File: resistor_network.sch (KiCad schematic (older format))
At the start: 0 parts

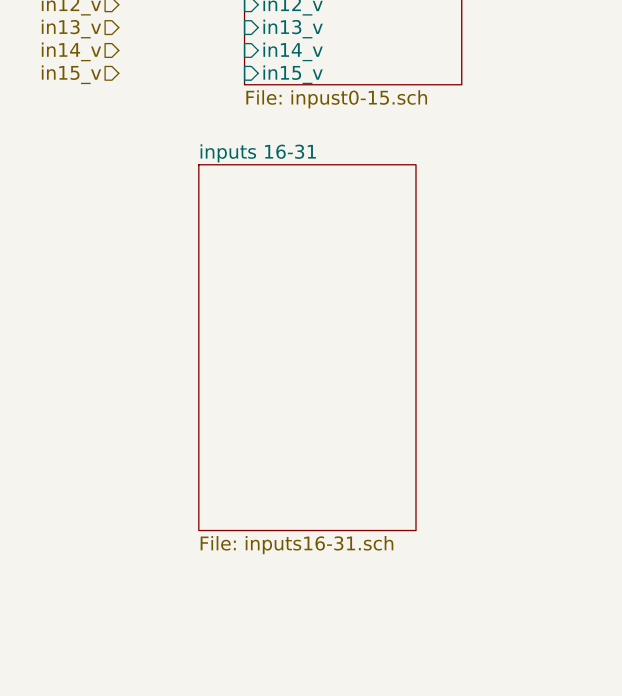
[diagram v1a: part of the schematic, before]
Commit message: added input/output for 16-31
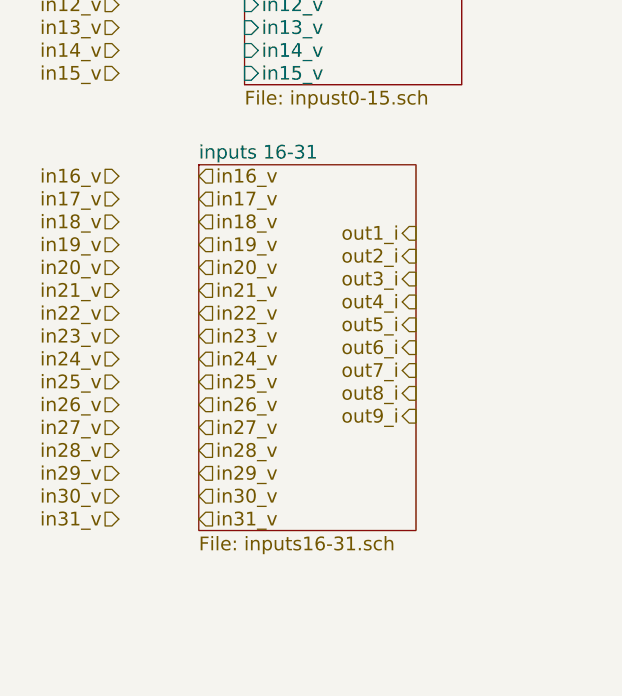
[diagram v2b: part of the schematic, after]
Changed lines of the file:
@@
 Text HLabel 1650 2600 0    60   Input ~ 0
 in15_v
+Text HLabel 1650 3050 0    60   Input ~ 0
+in16_v
+Text HLabel 1650 3150 0    60   Input ~ 0
+in17_v
+Text HLabel 1650 3250 0    60   Input ~ 0
+in18_v
+Text HLabel 1650 3350 0    60   Input ~ 0
+in19_v
+Text HLabel 1650 3450 0    60   Input ~ 0
+in20_v
+Text HLabel 1650 3550 0    60   Input ~ 0
+in21_v
+Text HLabel 1650 3650 0    60   Input ~ 0
+in22_v
+Text HLabel 1650 3750 0    60   Input ~ 0
+in23_v
+Text HLabel 1650 3850 0    60   Input ~ 0
+in24_v
+Text HLabel 1650 3950 0    60   Input ~ 0
+in25_v
+Text HLabel 1650 4050 0    60   Input ~ 0
+in26_v
+Text HLabel 1650 4150 0    60   Input ~ 0
+in27_v
+Text HLabel 1650 4250 0    60   Input ~ 0
+in28_v
+Text HLabel 1650 4350 0    60   Input ~ 0
+in29_v
+Text HLabel 1650 4450 0    60   Input ~ 0
+in30_v
+Text HLabel 1650 4550 0    60   Input ~ 0
+in31_v
+Text HLabel 2000 3050 2    60   Input ~ 0
+in16_v
+Text HLabel 2000 3150 2    60   Input ~ 0
+in17_v
+Text HLabel 2000 3250 2    60   Input ~ 0
+in18_v
+Text HLabel 2000 3350 2    60   Input ~ 0
+in19_v
+Text HLabel 2000 3450 2    60   Input ~ 0
+in20_v
+Text HLabel 2000 3550 2    60   Input ~ 0
+in21_v
+Text HLabel 2000 3650 2    60   Input ~ 0
+in22_v
+Text HLabel 2000 3750 2    60   Input ~ 0
+in23_v
+Text HLabel 2000 3850 2    60   Input ~ 0
+in24_v
+Text HLabel 2000 3950 2    60   Input ~ 0
+in25_v
+Text HLabel 2000 4050 2    60   Input ~ 0
+in26_v
+Text HLabel 2000 4150 2    60   Input ~ 0
+in27_v
+Text HLabel 2000 4250 2    60   Input ~ 0
+in28_v
+Text HLabel 2000 4350 2    60   Input ~ 0
+in29_v
+Text HLabel 2000 4450 2    60   Input ~ 0
+in30_v
+Text HLabel 2000 4550 2    60   Input ~ 0
+in31_v
+Text HLabel 2950 3300 0    60   Output ~ 0
+out1_i
+Text HLabel 2950 3400 0    60   Output ~ 0
+out2_i
+Text HLabel 2950 3500 0    60   Output ~ 0
+out3_i
+Text HLabel 2950 3600 0    60   Output ~ 0
+out4_i
+Text HLabel 2950 3700 0    60   Output ~ 0
+out5_i
+Text HLabel 2950 3800 0    60   Output ~ 0
+out6_i
+Text HLabel 2950 3900 0    60   Output ~ 0
+out7_i
+Text HLabel 2950 4000 0    60   Output ~ 0
+out8_i
+Text HLabel 2950 4100 0    60   Output ~ 0
+out9_i
 $EndSCHEMATC

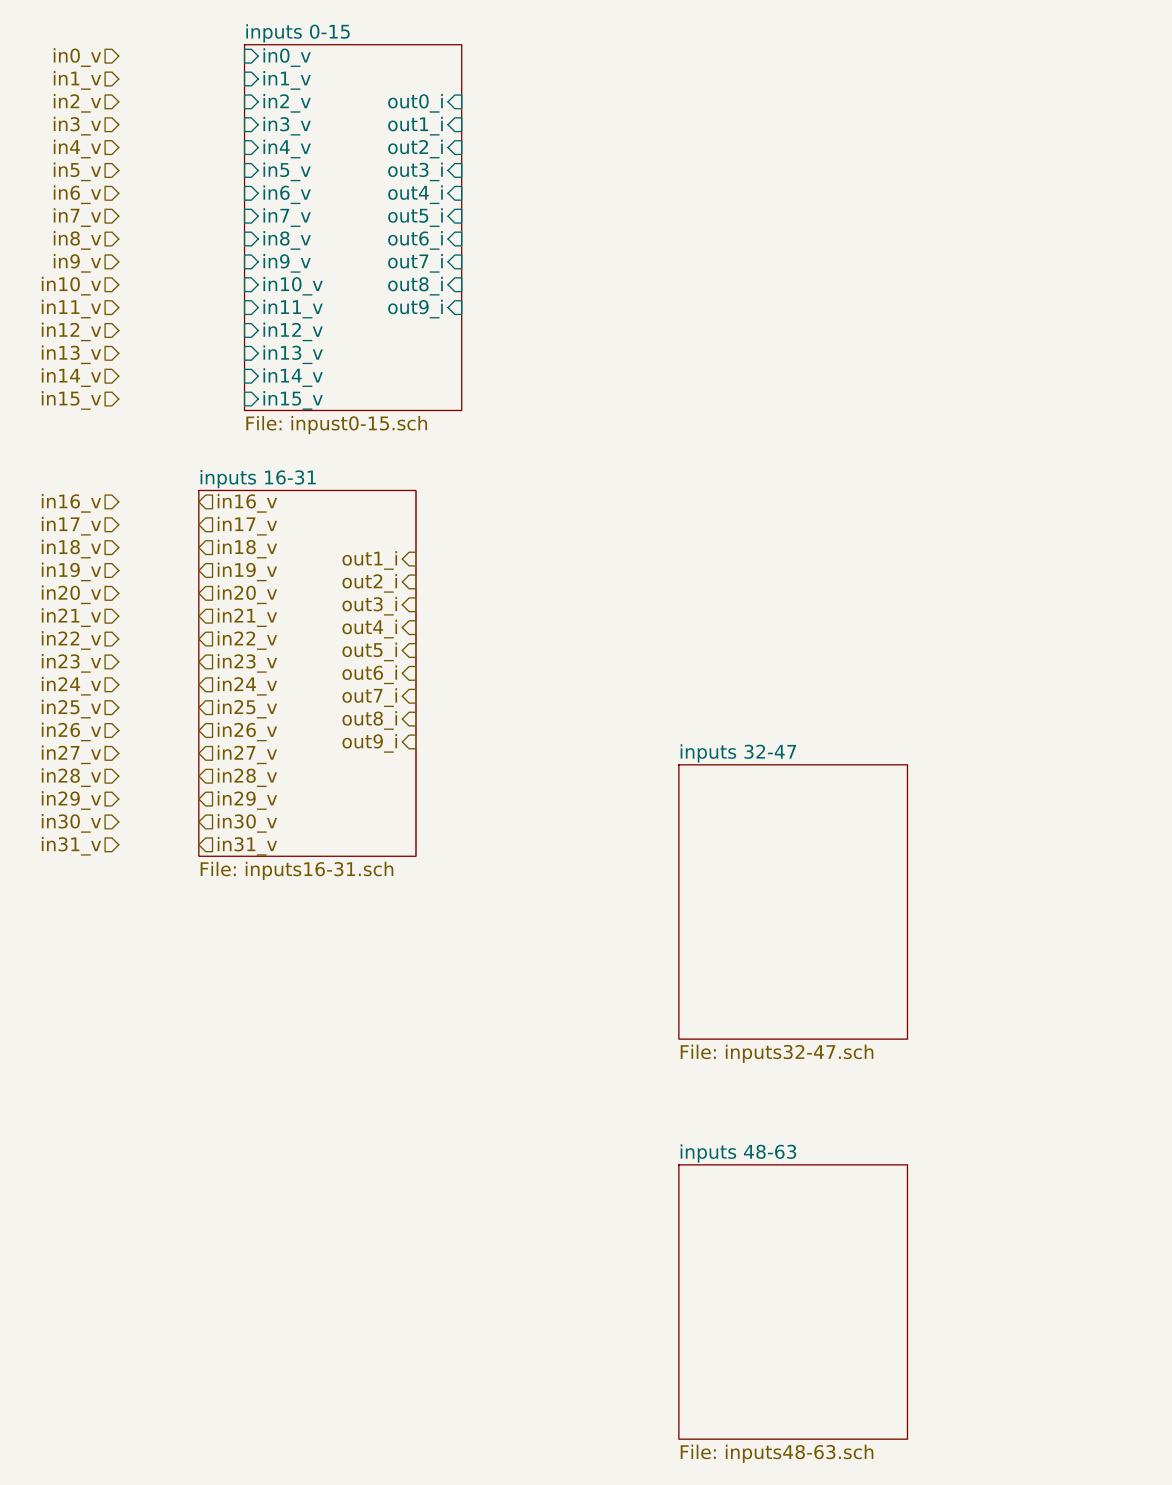
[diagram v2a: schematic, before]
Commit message: added labels
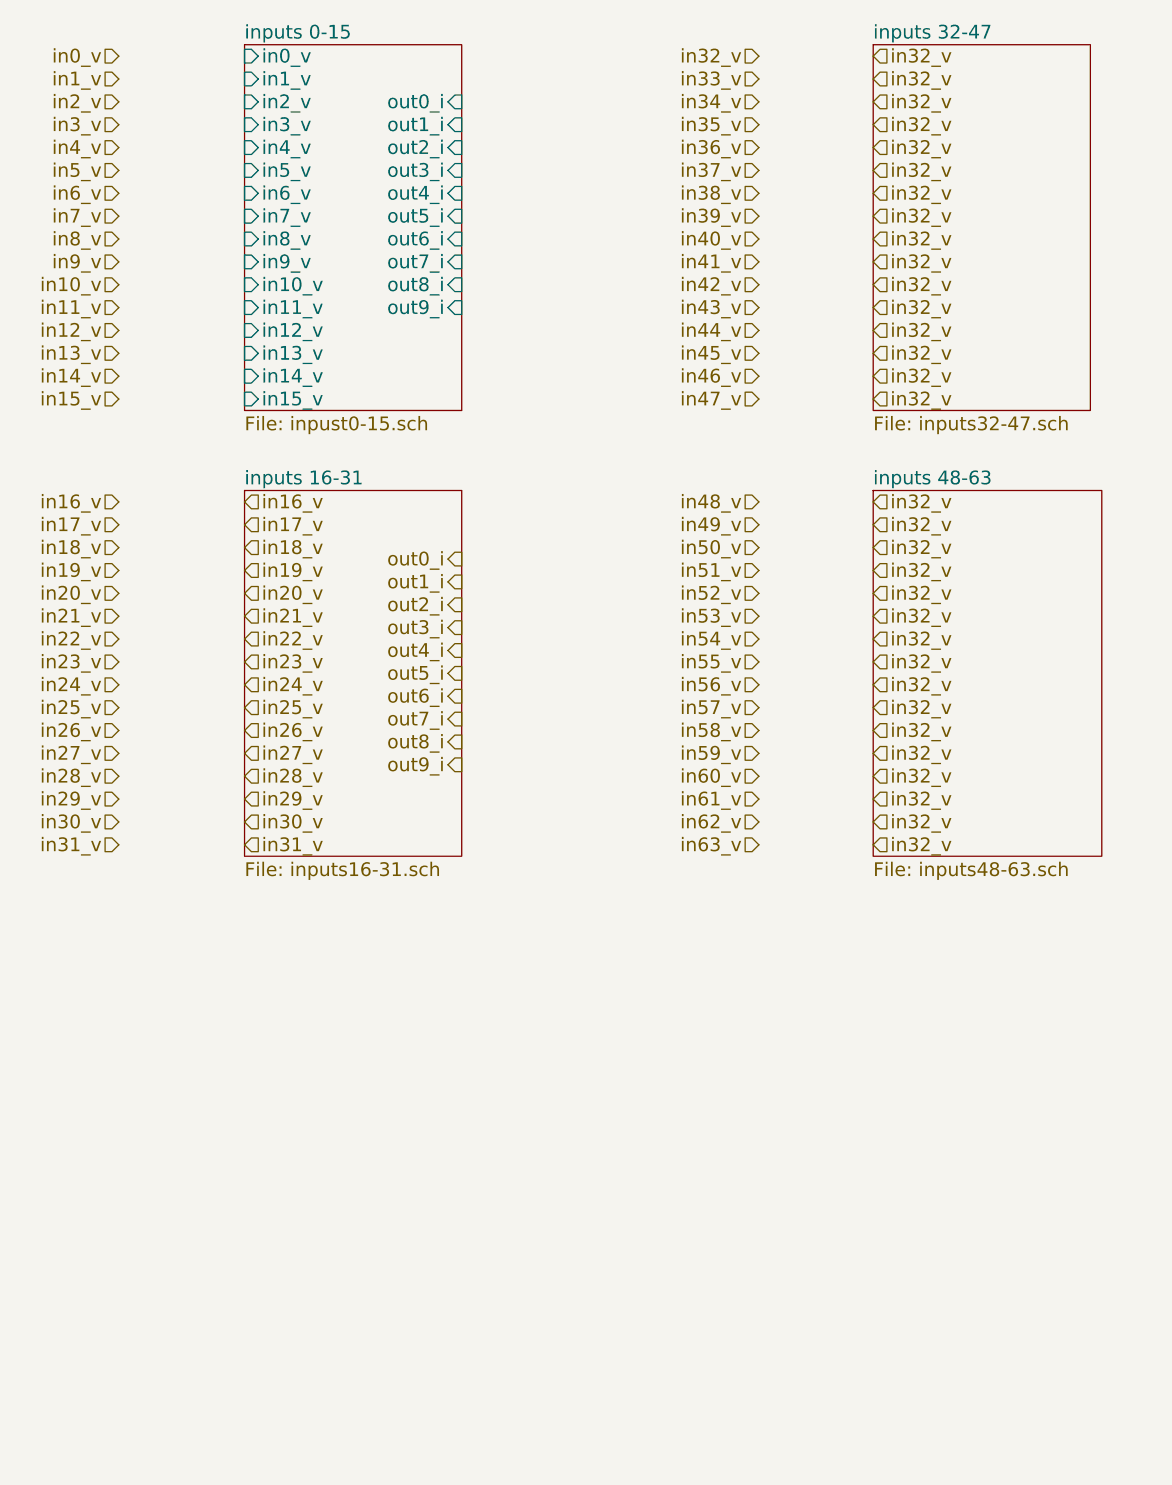
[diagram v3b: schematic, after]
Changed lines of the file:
@@
 $EndSheet
 $Sheet
-S 2000 3000 950  1600
+S 2200 3000 950  1600
 U 5C6CB74E
 F0 "inputs 16-31" 60
@@
 $EndSheet
 $Sheet
-S 4100 4200 1000 1200
+S 4950 1050 950  1600
 U 5C6CB753
 F0 "inputs 32-47" 60
@@
 $EndSheet
 $Sheet
-S 4100 5950 1000 1200
+S 4950 3000 1000 1600
 U 5C6CB756
 F0 "inputs 48-63" 60
@@
 Text HLabel 1650 4550 0    60   Input ~ 0
 in31_v
-Text HLabel 2000 3050 2    60   Input ~ 0
+Text HLabel 2200 3050 2    60   Input ~ 0
 in16_v
-Text HLabel 2000 3150 2    60   Input ~ 0
+Text HLabel 2200 3150 2    60   Input ~ 0
 in17_v
-Text HLabel 2000 3250 2    60   Input ~ 0
+Text HLabel 2200 3250 2    60   Input ~ 0
 in18_v
-Text HLabel 2000 3350 2    60   Input ~ 0
+Text HLabel 2200 3350 2    60   Input ~ 0
 in19_v
-Text HLabel 2000 3450 2    60   Input ~ 0
+Text HLabel 2200 3450 2    60   Input ~ 0
 in20_v
-Text HLabel 2000 3550 2    60   Input ~ 0
+Text HLabel 2200 3550 2    60   Input ~ 0
 in21_v
-Text HLabel 2000 3650 2    60   Input ~ 0
+Text HLabel 2200 3650 2    60   Input ~ 0
 in22_v
-Text HLabel 2000 3750 2    60   Input ~ 0
+Text HLabel 2200 3750 2    60   Input ~ 0
 in23_v
-Text HLabel 2000 3850 2    60   Input ~ 0
+Text HLabel 2200 3850 2    60   Input ~ 0
 in24_v
-Text HLabel 2000 3950 2    60   Input ~ 0
+Text HLabel 2200 3950 2    60   Input ~ 0
 in25_v
-Text HLabel 2000 4050 2    60   Input ~ 0
+Text HLabel 2200 4050 2    60   Input ~ 0
 in26_v
-Text HLabel 2000 4150 2    60   Input ~ 0
+Text HLabel 2200 4150 2    60   Input ~ 0
 in27_v
-Text HLabel 2000 4250 2    60   Input ~ 0
+Text HLabel 2200 4250 2    60   Input ~ 0
 in28_v
-Text HLabel 2000 4350 2    60   Input ~ 0
+Text HLabel 2200 4350 2    60   Input ~ 0
 in29_v
-Text HLabel 2000 4450 2    60   Input ~ 0
+Text HLabel 2200 4450 2    60   Input ~ 0
 in30_v
-Text HLabel 2000 4550 2    60   Input ~ 0
+Text HLabel 2200 4550 2    60   Input ~ 0
 in31_v
-Text HLabel 2950 3300 0    60   Output ~ 0
+Text HLabel 3150 3400 0    60   Output ~ 0
 out1_i
-Text HLabel 2950 3400 0    60   Output ~ 0
+Text HLabel 3150 3500 0    60   Output ~ 0
 out2_i
-Text HLabel 2950 3500 0    60   Output ~ 0
+Text HLabel 3150 3600 0    60   Output ~ 0
 out3_i
-Text HLabel 2950 3600 0    60   Output ~ 0
+Text HLabel 3150 3700 0    60   Output ~ 0
 out4_i
-Text HLabel 2950 3700 0    60   Output ~ 0
+Text HLabel 3150 3800 0    60   Output ~ 0
 out5_i
-Text HLabel 2950 3800 0    60   Output ~ 0
+Text HLabel 3150 3900 0    60   Output ~ 0
 out6_i
-Text HLabel 2950 3900 0    60   Output ~ 0
+Text HLabel 3150 4000 0    60   Output ~ 0
 out7_i
-Text HLabel 2950 4000 0    60   Output ~ 0
+Text HLabel 3150 4100 0    60   Output ~ 0
 out8_i
-Text HLabel 2950 4100 0    60   Output ~ 0
+Text HLabel 3150 4200 0    60   Output ~ 0
 out9_i
+Text HLabel 3150 3300 0    60   Output ~ 0
+out0_i
+Text HLabel 4450 1100 0    60   Input ~ 0
+in32_v
+Text HLabel 4450 1200 0    60   Input ~ 0
+in33_v
+Text HLabel 4450 1300 0    60   Input ~ 0
+in34_v
+Text HLabel 4450 1400 0    60   Input ~ 0
+in35_v
+Text HLabel 4450 1500 0    60   Input ~ 0
+in36_v
+Text HLabel 4450 1600 0    60   Input ~ 0
+in37_v
+Text HLabel 4450 1700 0    60   Input ~ 0
+in38_v
+Text HLabel 4450 1800 0    60   Input ~ 0
+in39_v
+Text HLabel 4450 1900 0    60   Input ~ 0
+in40_v
+Text HLabel 4450 2000 0    60   Input ~ 0
+in41_v
+Text HLabel 4450 2100 0    60   Input ~ 0
+in42_v
+Text HLabel 4450 2200 0    60   Input ~ 0
+in43_v
+Text HLabel 4450 2300 0    60   Input ~ 0
+in44_v
+Text HLabel 4450 2400 0    60   Input ~ 0
+in45_v
+Text HLabel 4450 2500 0    60   Input ~ 0
+in46_v
+Text HLabel 4450 2600 0    60   Input ~ 0
+in47_v
+Text HLabel 4450 3150 0    60   Input ~ 0
+in49_v
+Text HLabel 4450 3050 0    60   Input ~ 0
+in48_v
+Text HLabel 4450 3250 0    60   Input ~ 0
+in50_v
+Text HLabel 4450 3350 0    60   Input ~ 0
+in51_v
+Text HLabel 4450 3450 0    60   Input ~ 0
+in52_v
+Text HLabel 4450 3550 0    60   Input ~ 0
+in53_v
+Text HLabel 4450 3650 0    60   Input ~ 0
+in54_v
+Text HLabel 4450 3750 0    60   Input ~ 0
+in55_v
+Text HLabel 4450 3850 0    60   Input ~ 0
+in56_v
+Text HLabel 4450 3950 0    60   Input ~ 0
+in57_v
+Text HLabel 4450 4050 0    60   Input ~ 0
+in58_v
+Text HLabel 4450 4150 0    60   Input ~ 0
+in59_v
+Text HLabel 4450 4250 0    60   Input ~ 0
+in60_v
+Text HLabel 4450 4350 0    60   Input ~ 0
+in61_v
+Text HLabel 4450 4450 0    60   Input ~ 0
+in62_v
+Text HLabel 4450 4550 0    60   Input ~ 0
+in63_v
+Text HLabel 4950 1100 2    60   Input ~ 0
+in32_v
+Text HLabel 4950 1200 2    60   Input ~ 0
+in32_v
+Text HLabel 4950 1300 2    60   Input ~ 0
+in32_v
+Text HLabel 4950 1400 2    60   Input ~ 0
+in32_v
+Text HLabel 4950 1500 2    60   Input ~ 0
+in32_v
+Text HLabel 4950 1600 2    60   Input ~ 0
+in32_v
+Text HLabel 4950 1700 2    60   Input ~ 0
+in32_v
+Text HLabel 4950 1800 2    60   Input ~ 0
+in32_v
+Text HLabel 4950 1900 2    60   Input ~ 0
+in32_v
+Text HLabel 4950 2000 2    60   Input ~ 0
+in32_v
+Text HLabel 4950 2100 2    60   Input ~ 0
+in32_v
+Text HLabel 4950 2200 2    60   Input ~ 0
+in32_v
+Text HLabel 4950 2300 2    60   Input ~ 0
+in32_v
+Text HLabel 4950 2400 2    60   Input ~ 0
+in32_v
+Text HLabel 4950 2500 2    60   Input ~ 0
+in32_v
+Text HLabel 4950 2600 2    60   Input ~ 0
+in32_v
+Text HLabel 4950 3050 2    60   Input ~ 0
+in32_v
+Text HLabel 4950 3150 2    60   Input ~ 0
+in32_v
+Text HLabel 4950 3250 2    60   Input ~ 0
+in32_v
+Text HLabel 4950 3350 2    60   Input ~ 0
+in32_v
+Text HLabel 4950 3450 2    60   Input ~ 0
+in32_v
+Text HLabel 4950 3550 2    60   Input ~ 0
+in32_v
+Text HLabel 4950 3650 2    60   Input ~ 0
+in32_v
+Text HLabel 4950 3750 2    60   Input ~ 0
+in32_v
+Text HLabel 4950 3850 2    60   Input ~ 0
+in32_v
+Text HLabel 4950 3950 2    60   Input ~ 0
+in32_v
+Text HLabel 4950 4050 2    60   Input ~ 0
+in32_v
+Text HLabel 4950 4150 2    60   Input ~ 0
+in32_v
+Text HLabel 4950 4250 2    60   Input ~ 0
+in32_v
+Text HLabel 4950 4350 2    60   Input ~ 0
+in32_v
+Text HLabel 4950 4450 2    60   Input ~ 0
+in32_v
+Text HLabel 4950 4550 2    60   Input ~ 0
+in32_v
 $EndSCHEMATC
